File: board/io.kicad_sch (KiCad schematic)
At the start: 10 parts, among them J2 KEYBOARD, J4 MOUSE, J9 FTDI serial, U16 AT89x51xxP, Y2 11.0592MHz

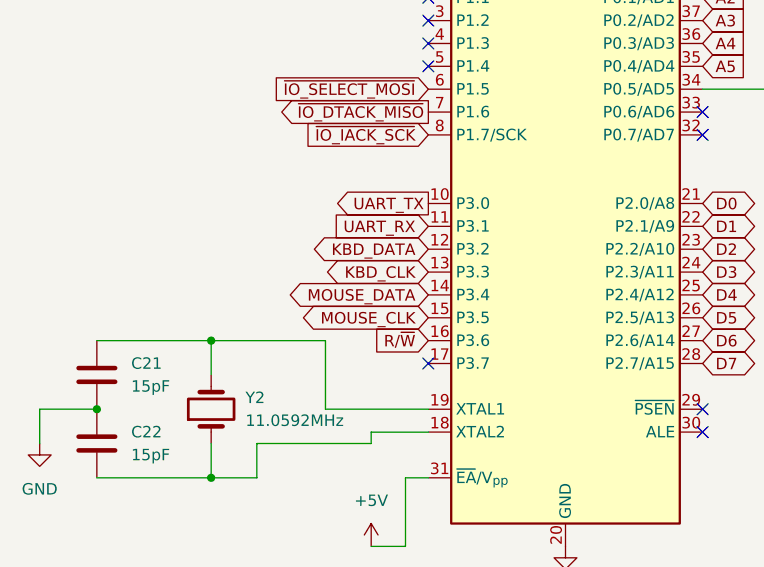
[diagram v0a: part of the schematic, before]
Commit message: update JTAG bypass and 8051 PS/2 pins
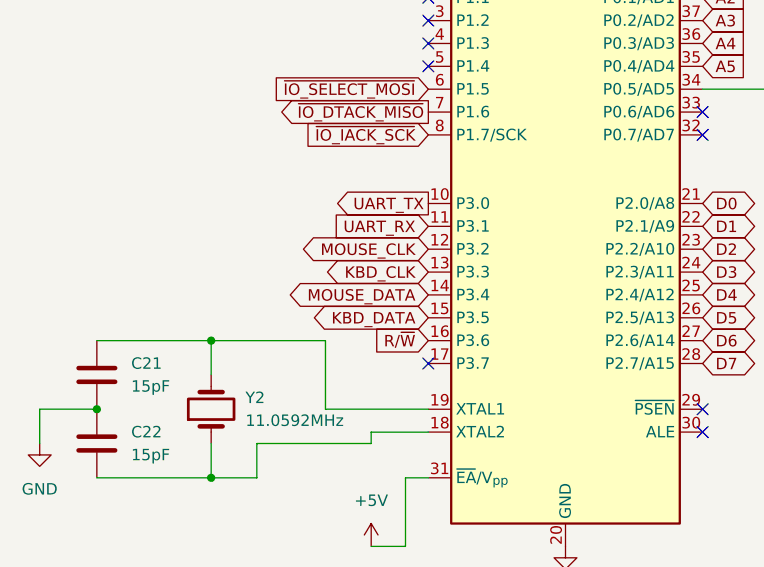
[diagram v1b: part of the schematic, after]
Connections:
- net KBD_DATA: now also U16.15 (P3.5); no longer U16.12 (P3.2)
- net MOUSE_CLK: now also U16.12 (P3.2); no longer U16.15 (P3.5)
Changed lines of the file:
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@@
 	(global_label "MOUSE_CLK"
 		(shape bidirectional)
-		(at 59.69 115.57 180)
+		(at 59.69 107.95 180)
 		(fields_autoplaced yes)
 		(effects
@@
 		)
 		(property "Intersheetrefs" "${INTERSHEET_REFS}"
-			(at 44.5869 115.57 0)
+			(at 44.5869 107.95 0)
 			(effects
 				(font
@@
 	(global_label "KBD_DATA"
 		(shape bidirectional)
-		(at 59.69 107.95 180)
+		(at 59.69 115.57 180)
 		(fields_autoplaced yes)
 		(effects
@@
 		)
 		(property "Intersheetrefs" "${INTERSHEET_REFS}"
-			(at 46.4011 107.95 0)
+			(at 46.4011 115.57 0)
 			(effects
 				(font
